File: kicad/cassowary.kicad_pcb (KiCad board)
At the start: 2 copper layers, 198.6 x 102.1 mm, 19 parts, among them U1 Pico

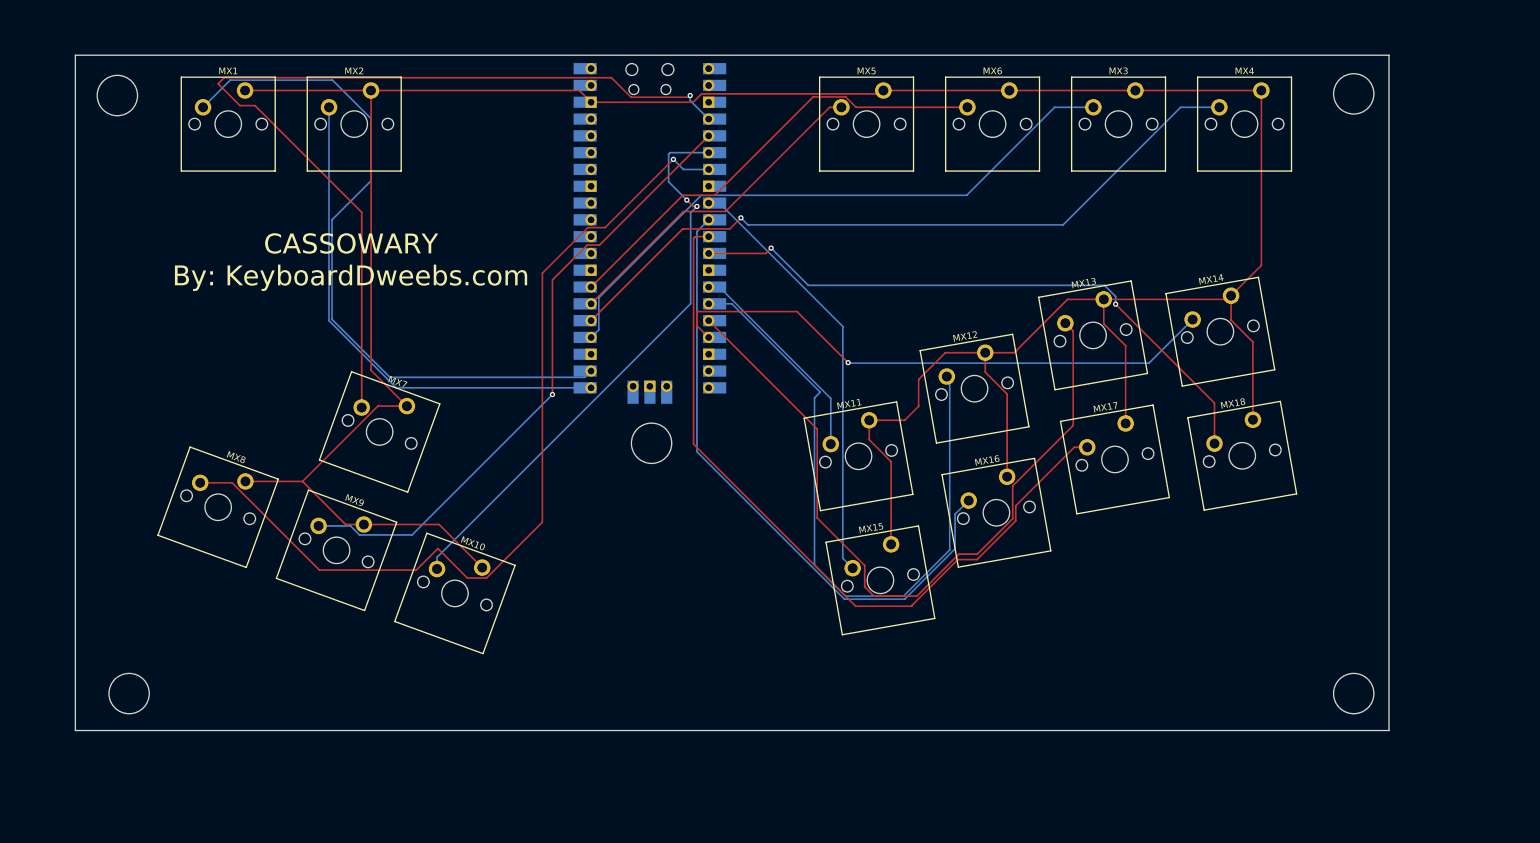
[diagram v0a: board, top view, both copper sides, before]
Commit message: add thumb key and fill
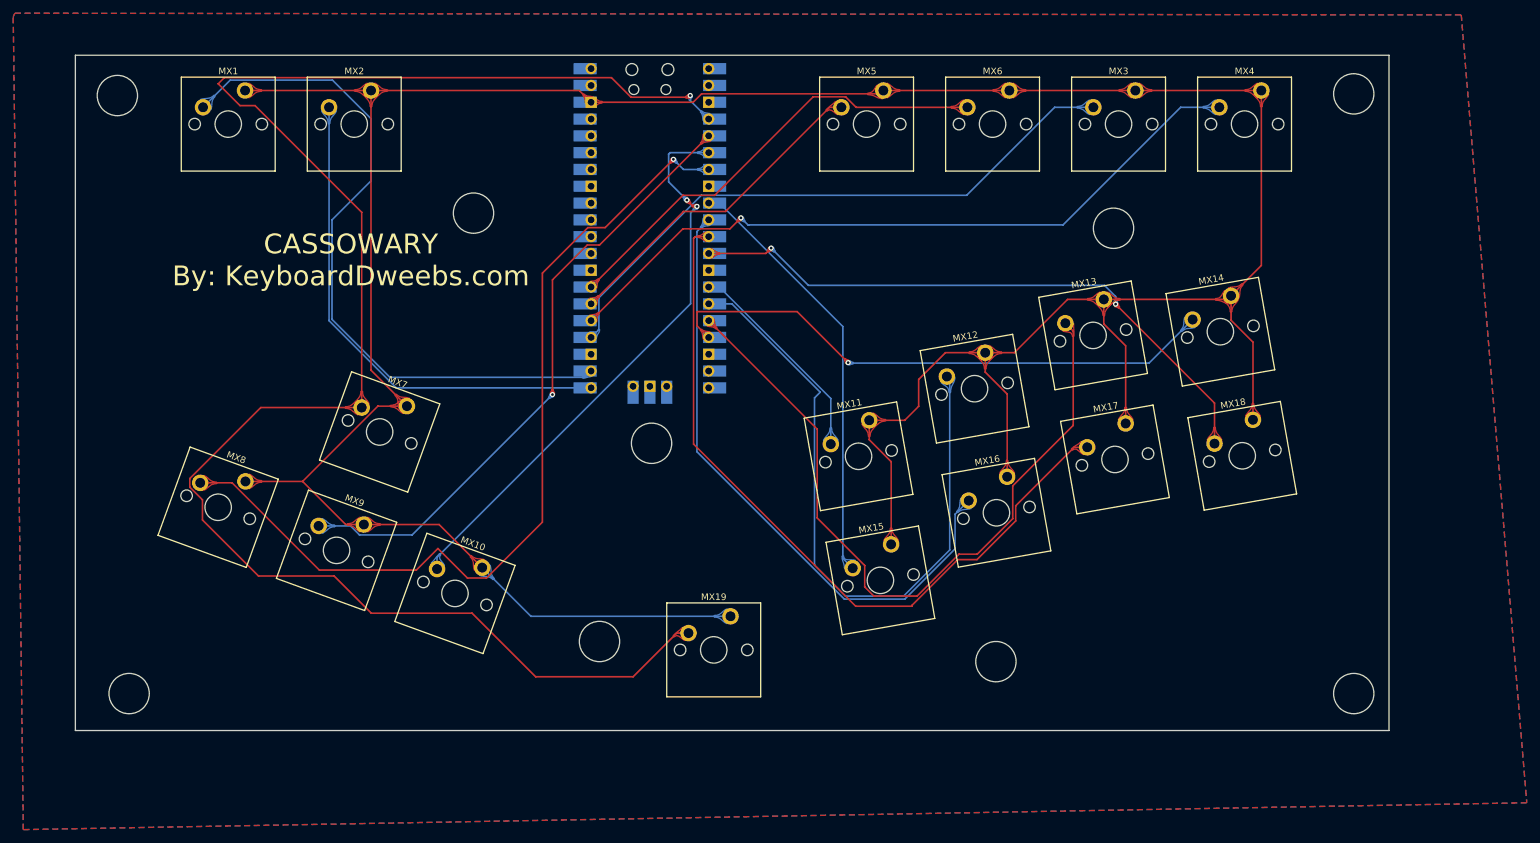
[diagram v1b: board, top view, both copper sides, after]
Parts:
- added MX19: MX-NoLED, Switch_Keyboard_Cherry_MX:SW_Cherry_MX_PCB_1.00u, F.Cu at (154.2, 137.4)
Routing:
- net UP: track 137.1 -> 260.6 mm
- net GND: track 445.2 -> 485.7 mm
- added copper zone on B.Cu, net (none)
- added copper zone on F.Cu, net (none)
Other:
- outline, holes or cut-outs redrawn
